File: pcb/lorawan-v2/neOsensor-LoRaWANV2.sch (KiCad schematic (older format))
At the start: 29 parts, among them J1 Conn_01x05, J2 Conn_01x02, J3 Conn_01x05, J4 Conn_01x04, J5 Conn_01x05, J6 Conn_01x05, J7 Conn_01x05, SW1 G71Y, U1 OLED1.3_I2C, U2 ATECC508A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

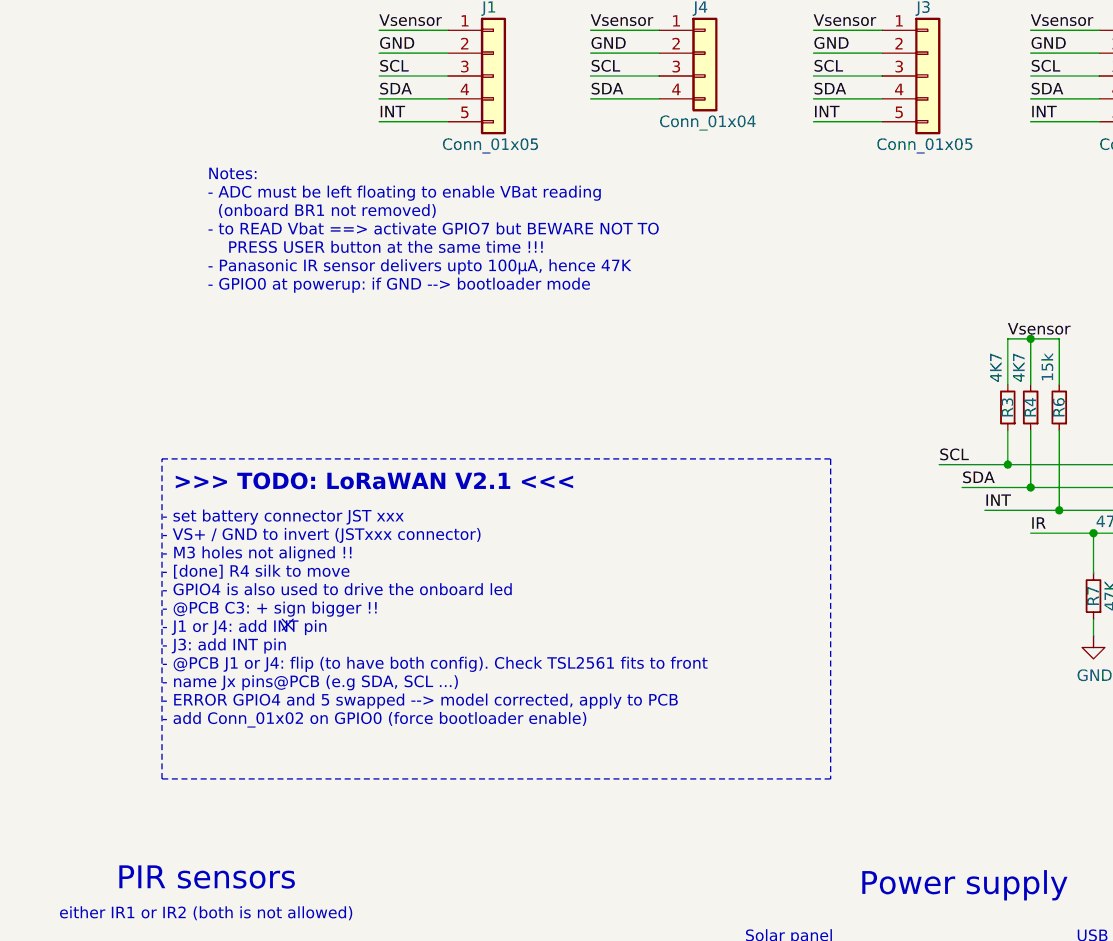
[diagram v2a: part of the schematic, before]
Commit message: new LoRaWAN V2.1 sent to manufacturing
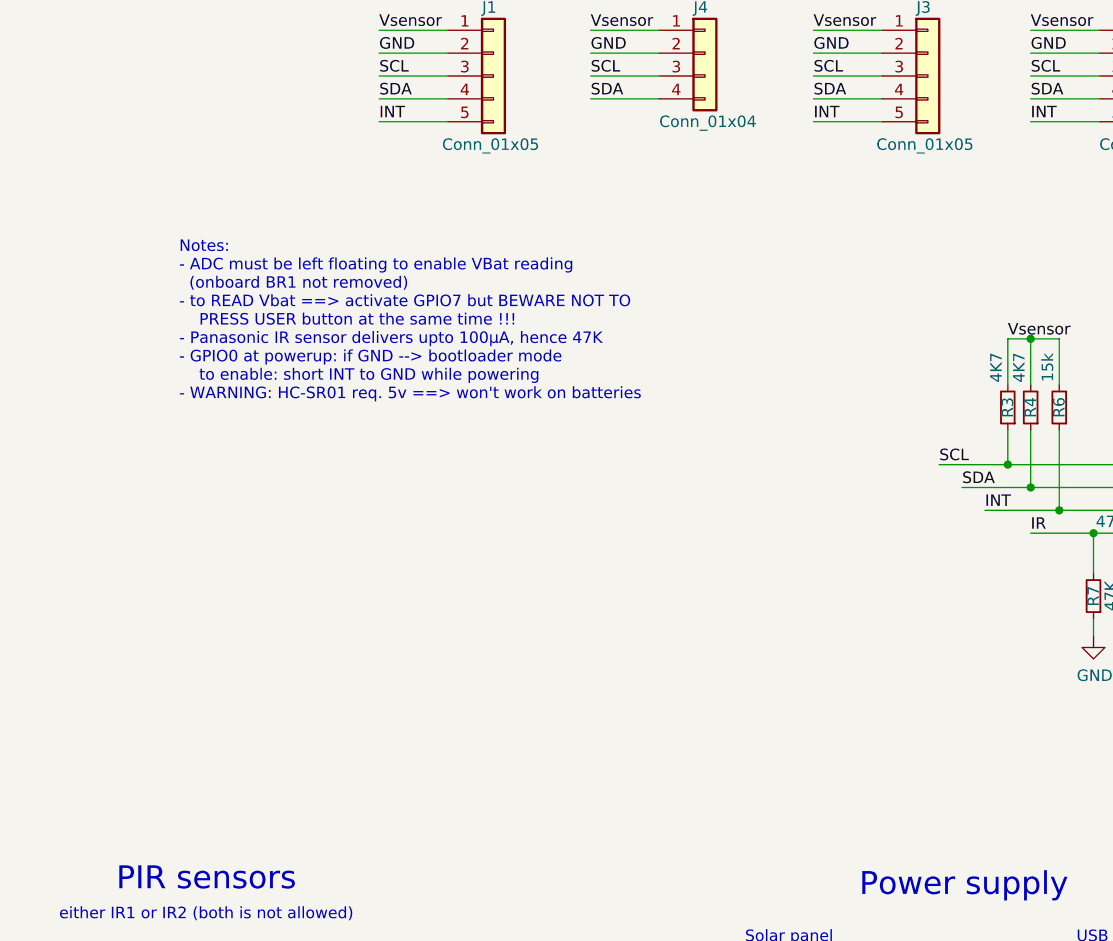
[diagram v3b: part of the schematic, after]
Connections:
- no-connect marks 9 -> 8
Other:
- note added: "Notes:\n- ADC must be left floating to enable VBat reading\n (onboard BR1 not removed)\n- to READ Vbat ==> activate GPIO7 but BEWARE NOT TO\n PRESS USER button at the same time !!!\n- Panasonic IR sensor delivers upto 100µA, hence 47K\n- GPIO0 at powerup: if GND --> bootloader mode\n to enable: short INT to GND while powering\n- WARNING: HC-SR01 req. 5v ==> won't work on batteries"
- note removed: "- set battery connector JST xxx\n- VS+ / GND to invert (JSTxxx connector)\n- M3 holes not aligned !!\n- [done] R4 silk to move\n- GPIO4 is also used to drive the onboard led\n- @PCB C3: + sign bigger !!\n- J1 or J4: add INT pin\n- J3: add INT pin\n- @PCB J1 or J4: flip (to have both config). Check TSL2561 fits to front\n- name Jx pins@PCB (e.g SDA, SCL ...)\n- ERROR GPIO4 and 5 swapped --> model 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"
- note removed: ">>> TODO: LoRaWAN V2.1 <<<"
- note removed: "Notes:\n- ADC must be left floating to enable VBat reading\n (onboard BR1 not removed)\n- to READ Vbat ==> activate GPIO7 but BEWARE NOT TO\n PRESS USER button at the same time !!!\n- Panasonic IR sensor delivers upto 100µA, hence 47K\n- GPIO0 at powerup: if GND --> bootloader mode"
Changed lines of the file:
@@
 Text Notes 6250 4800 0    100  ~ 0
 Power supply
-Text Notes 3400 2150 0    50   ~ 0
-Notes:\n- ADC must be left floating to enable VBat reading\n  (onboard BR1 not removed)\n- to READ Vbat ==> activate GPIO7 but BEWARE NOT TO\n    PRESS USER button at the same time !!!\n- Panasonic IR sensor delivers upto 100µA, hence 47K\n- GPIO0 at powerup: if GND --> bootloader mode
+Text Notes 3275 2625 0    50   ~ 0
+Notes:\n- ADC must be left floating to enable VBat reading\n  (onboard BR1 not removed)\n- to READ Vbat ==> activate GPIO7 but BEWARE NOT TO\n    PRESS USER button at the same time !!!\n- Panasonic IR sensor delivers upto 100µA, hence 47K\n- GPIO0 at powerup: if GND --> bootloader mode\n    to enable: short INT to GND while powering\n- WARNING: HC-SR01 req. 5v ==> won't work on batteries
 $Comp
 L Device:C_Small C2
@@
 Wire Wire Line
 	1750 1300 1700 1300
-Wire Notes Line
-	3200 2875 6125 2875
-Wire Notes Line
-	6125 2875 6125 4275
-Wire Notes Line
-	6125 4275 3200 4275
-Wire Notes Line
-	3200 4275 3200 2875
-Text Notes 3250 3025 0    71   ~ 14
->>> TODO: LoRaWAN V2.1 <<<
-Text Notes 3200 4050 0    50   ~ 0
-- set battery connector JST xxx\n- VS+ / GND to invert (JSTxxx connector)\n- M3 holes not aligned !!\n- [done] R4 silk to move\n- GPIO4 is also used to drive the onboard led\n- @PCB C3: + sign bigger !!\n- J1 or J4: add INT pin\n- J3: add INT pin\n- @PCB J1 or J4: flip (to have both config). Check TSL2561 fits to front\n- name Jx pins@PCB (e.g SDA, SCL ...)\n- ERROR GPIO4 and 5 swapped --> model corrected, apply to PCB\n- add Conn_01x02 on GPIO0 (force bootloader enable)
 Wire Wire Line
 	7000 2350 7125 2350
@@
 SW1
 NoConn ~ 8700 3200
-NoConn ~ 3750 3600
 $Comp
 L Connector_Generic:Conn_01x05 J3
